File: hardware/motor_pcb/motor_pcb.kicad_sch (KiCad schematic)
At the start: 13 parts

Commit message: Updated schematic
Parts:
- removed J?: Conn_01x13, symbol Connector_Generic:Conn_01x13
- added J1: Conn_01x14, Connector_Hirose:Hirose_DF52-14S-0.8H_1x14-1MP_P0.80mm_Horizontal, symbol Connector_Generic:Conn_01x14
- C1: renamed from C?; footprint (none) -> Capacitor_SMD:C_0805_2012Metric
- C2, C3, C4, C5, C6: renamed from C?; footprint (none) -> Capacitor_SMD:C_0603_1608Metric
- J2: renamed from J?; footprint (none) -> Connector_Hirose:Hirose_DF52-3S-0.8H_1x03-1MP_P0.80mm_Horizontal; LCSC (none) -> C500138
- R1: renamed from R?; value R -> 0.15; footprint (none) -> Resistor_SMD:R_1206_3216Metric
- R2, R3: renamed from R?; footprint (none) -> Resistor_SMD:R_0603_1608Metric
- U1: renamed from U?; footprint Modified:QFN-20-1EP_3x3mm_P0.4mm_EP1.65x1.65mm_ThermalVias_LargerViaHoles -> Package_DFN_QFN:QFN-20-1EP_3x3mm_P0.4mm_EP1.65x1.65mm_ThermalVias
- gave numbers to parts that had none: 1
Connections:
- net +3V3: now also J1.1 (Pin_1)
- net +5V: now also J1.2 (Pin_2)
- net CS: now also J1.12 (Pin_12)
- net DIAG: now also J1.9 (Pin_9)
- net GND: now also J1.13 (Pin_13), J1.14 (Pin_14)
- net SCL: now also J1.11 (Pin_11)
- net SDA: now also J1.10 (Pin_10)
- net UH: now also J1.3 (Pin_3)
- net UL: now also J1.4 (Pin_4)
- net VH: now also J1.5 (Pin_5)
- net VL: now also J1.6 (Pin_6)
- net WH: now also J1.7 (Pin_7)
- net WL: now also J1.8 (Pin_8)
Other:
- note added: "0.15 Ohm -> 1.6A max motor current"

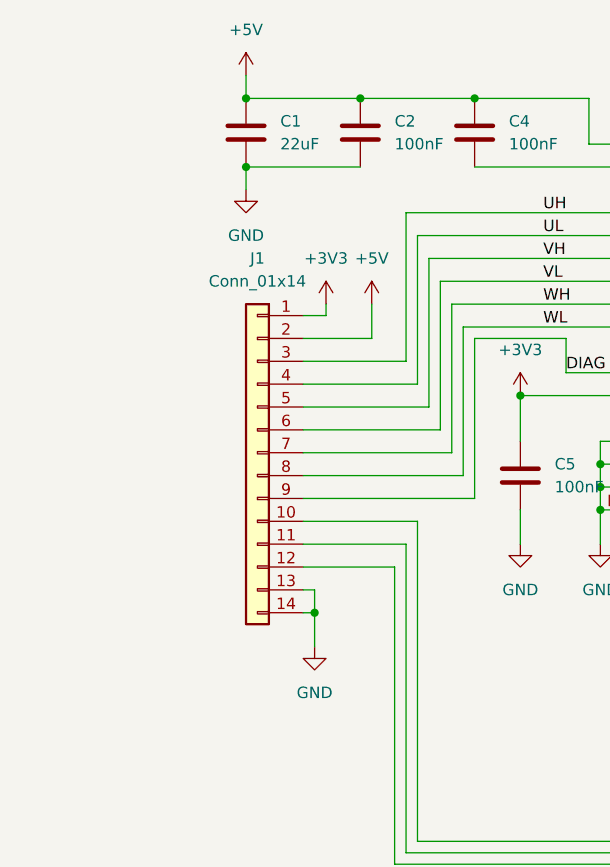
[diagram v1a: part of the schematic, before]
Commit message: Updated power connector
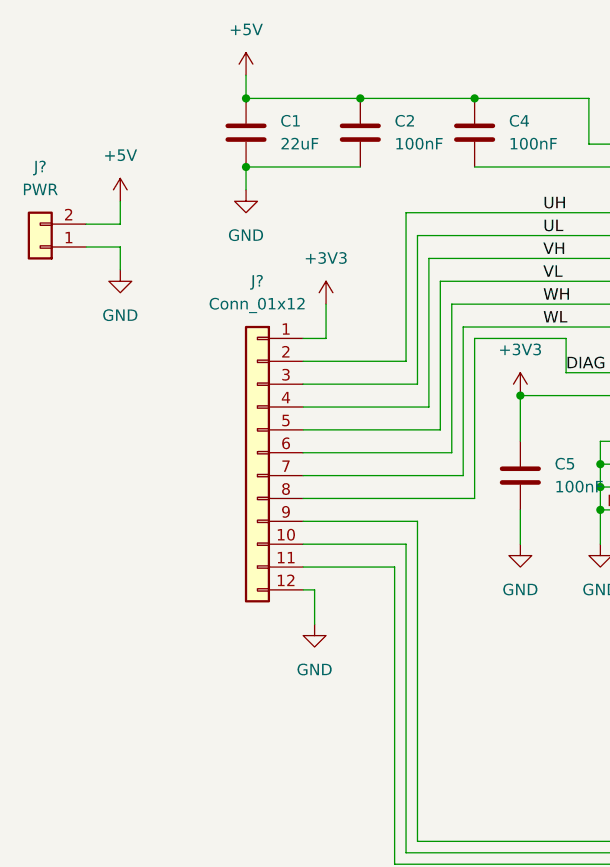
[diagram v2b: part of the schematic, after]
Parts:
- removed J1: Conn_01x14, Connector_Hirose:Hirose_DF52-14S-0.8H_1x14-1MP_P0.80mm_Horizontal, symbol Connector_Generic:Conn_01x14
- added J?: PWR, Connector_PinHeader_2.54mm:PinHeader_1x02_P2.54mm_Vertical, symbol Connector_Generic:Conn_01x02
- added J?: Conn_01x12, Connector_Hirose:Hirose_DF52-12S-0.8H_1x12-1MP_P0.80mm_Horizontal, symbol Connector_Generic:Conn_01x12
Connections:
- net +3V3: now also J?.1 (Pin_1)
- net +5V: now also J?.2 (Pin_2)
- net CS: now also J?.11 (Pin_11)
- net DIAG: now also J?.8 (Pin_8)
- net GND: now also J?.1 (Pin_1), J?.12 (Pin_12)
- net SCL: now also J?.10 (Pin_10)
- net SDA: now also J?.9 (Pin_9)
- net UH: now also J?.2 (Pin_2)
- net UL: now also J?.3 (Pin_3)
- net VH: now also J?.4 (Pin_4)
- net VL: now also J?.5 (Pin_5)
- net WH: now also J?.6 (Pin_6)
- net WL: now also J?.7 (Pin_7)

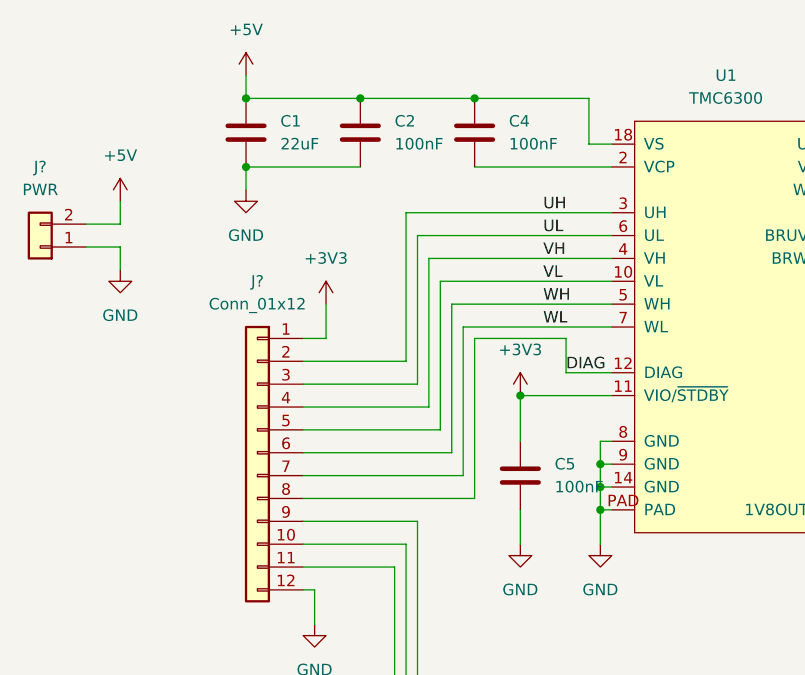
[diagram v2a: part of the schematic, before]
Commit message: Changed to fpc connector
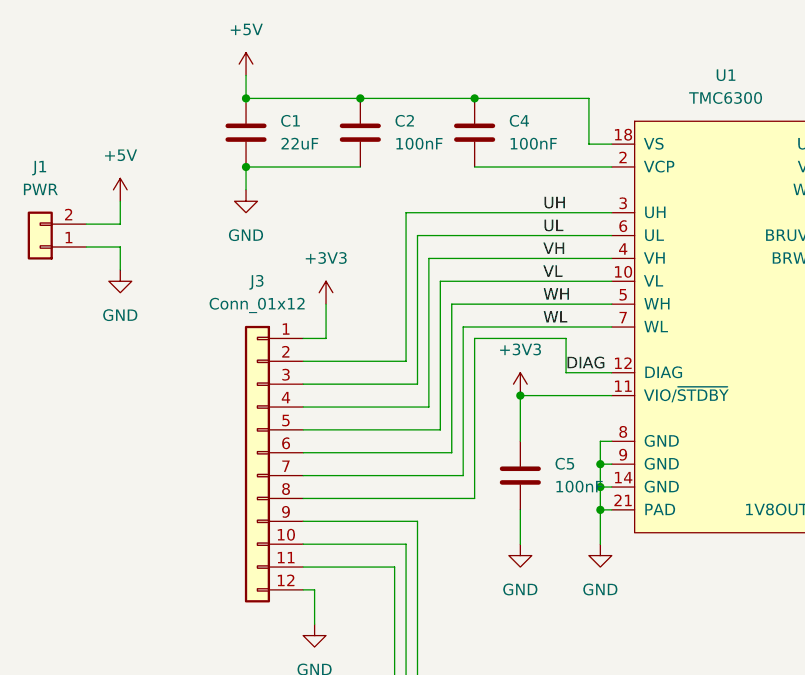
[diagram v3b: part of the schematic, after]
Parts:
- J3: renamed from J?; footprint Connector_Hirose:Hirose_DF52-12S-0.8H_1x12-1MP_P0.80mm_Horizontal -> Jushuo:FPC_12
- gave numbers to parts that had none: 1
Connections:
- net GND: now also U1.21 (PAD); no longer U1.PAD
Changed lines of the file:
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@@
   (symbol (lib_id "Connector_Generic:Conn_01x02") (at 88.9 45.72 180) (unit 1)
     (in_bom yes) (on_board yes) (fields_autoplaced)
-    (property "Reference" "J?" (id 0) (at 88.9 36.83 0))
+    (property "Reference" "J1" (id 0) (at 88.9 36.83 0))
     (property "Value" "PWR" (id 1) (at 88.9 39.37 0))
     (property "Footprint" "Connector_PinHeader_2.54mm:PinHeader_1x02_P2.54mm_Vertical" (id 2) (at 88.9 45.72 0)
@@
   (symbol (lib_id "power:GND") (at 97.79 48.26 0) (unit 1)
     (in_bom yes) (on_board yes) (fields_autoplaced)
-    (property "Reference" "#PWR?" (id 0) (at 97.79 54.61 0)
+    (property "Reference" "#PWR0101" (id 0) (at 97.79 54.61 0)
       (effects (font (size 1.27 1.27)) hide)
     )
@@
   (symbol (lib_id "Connector_Generic:Conn_01x12") (at 113.03 68.58 0) (mirror y) (unit 1)
     (in_bom yes) (on_board yes) (fields_autoplaced)
-    (property "Reference" "J?" (id 0) (at 113.03 49.53 0))
+    (property "Reference" "J3" (id 0) (at 113.03 49.53 0))
     (property "Value" "Conn_01x12" (id 1) (at 113.03 52.07 0))
-    (property "Footprint" "Connector_Hirose:Hirose_DF52-12S-0.8H_1x12-1MP_P0.80mm_Horizontal" (id 2) (at 113.03 68.58 0)
+    (property "Footprint" "Jushuo:FPC_12" (id 2) (at 113.03 68.58 0)
       (effects (font (size 1.27 1.27)) hide)
     )
@@
     (pin "8")
     (pin "9")
-    (pin "PAD")
+    (pin "21")
   )
   (symbol (lib_id "power:GND") (at 143.51 134.62 0) (unit 1)
@@
     )
     (path "/24612733-1d50-42bd-841c-be1f707d056b"
-      (reference "#PWR?") (unit 1) (value "GND") (footprint "")
+      (reference "#PWR0101") (unit 1) (value "GND") (footprint "")
     )
     (path "/8c77fd94-8e4c-4959-8bd9-3052e0edb37f"
@@
       (reference "C6") (unit 1) (value "100nF") (footprint "Capacitor_SMD:C_0603_1608Metric")
     )
+    (path "/03910351-5c5a-4e87-ae00-e0f31c977d99"
+      (reference "J1") (unit 1) (value "PWR") (footprint "Connector_PinHeader_2.54mm:PinHeader_1x02_P2.54mm_Vertical")
+    )
     (path "/a2c13c1a-ecf0-4489-bc67-4ea2d4323322"
       (reference "J2") (unit 1) (value "Conn_01x03") (footprint "Connector_Hirose:Hirose_DF52-3S-0.8H_1x03-1MP_P0.80mm_Horizontal")
     )
-    (path "/03910351-5c5a-4e87-ae00-e0f31c977d99"
-      (reference "J?") (unit 1) (value "PWR") (footprint "Connector_PinHeader_2.54mm:PinHeader_1x02_P2.54mm_Vertical")
-    )
     (path "/beeb3293-b654-424e-b1ea-63ed0fc7ea2d"
-      (reference "J?") (unit 1) (value "Conn_01x12") (footprint "Connector_Hirose:Hirose_DF52-12S-0.8H_1x12-1MP_P0.80mm_Horizontal")
+      (reference "J3") (unit 1) (value "Conn_01x12") (footprint "Jushuo:FPC_12")
     )
     (path "/ef183a37-aa63-490e-aeb2-ec1d529f6328"

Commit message: Updated lcsc number
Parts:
- J3: LCSC C3012324 -> C11051
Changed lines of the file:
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@@
       (effects (font (size 1.27 1.27)) hide)
     )
-    (property "LCSC" "C3012324" (id 4) (at 113.03 68.58 0)
+    (property "LCSC" "C11051" (id 4) (at 113.03 68.58 0)
       (effects (font (size 1.27 1.27)) hide)
     )
@@
     (pin "2")
     (pin "20")
+    (pin "21")
     (pin "3")
     (pin "4")
@@
     (pin "8")
     (pin "9")
-    (pin "21")
   )
   (symbol (lib_id "power:GND") (at 143.51 134.62 0) (unit 1)

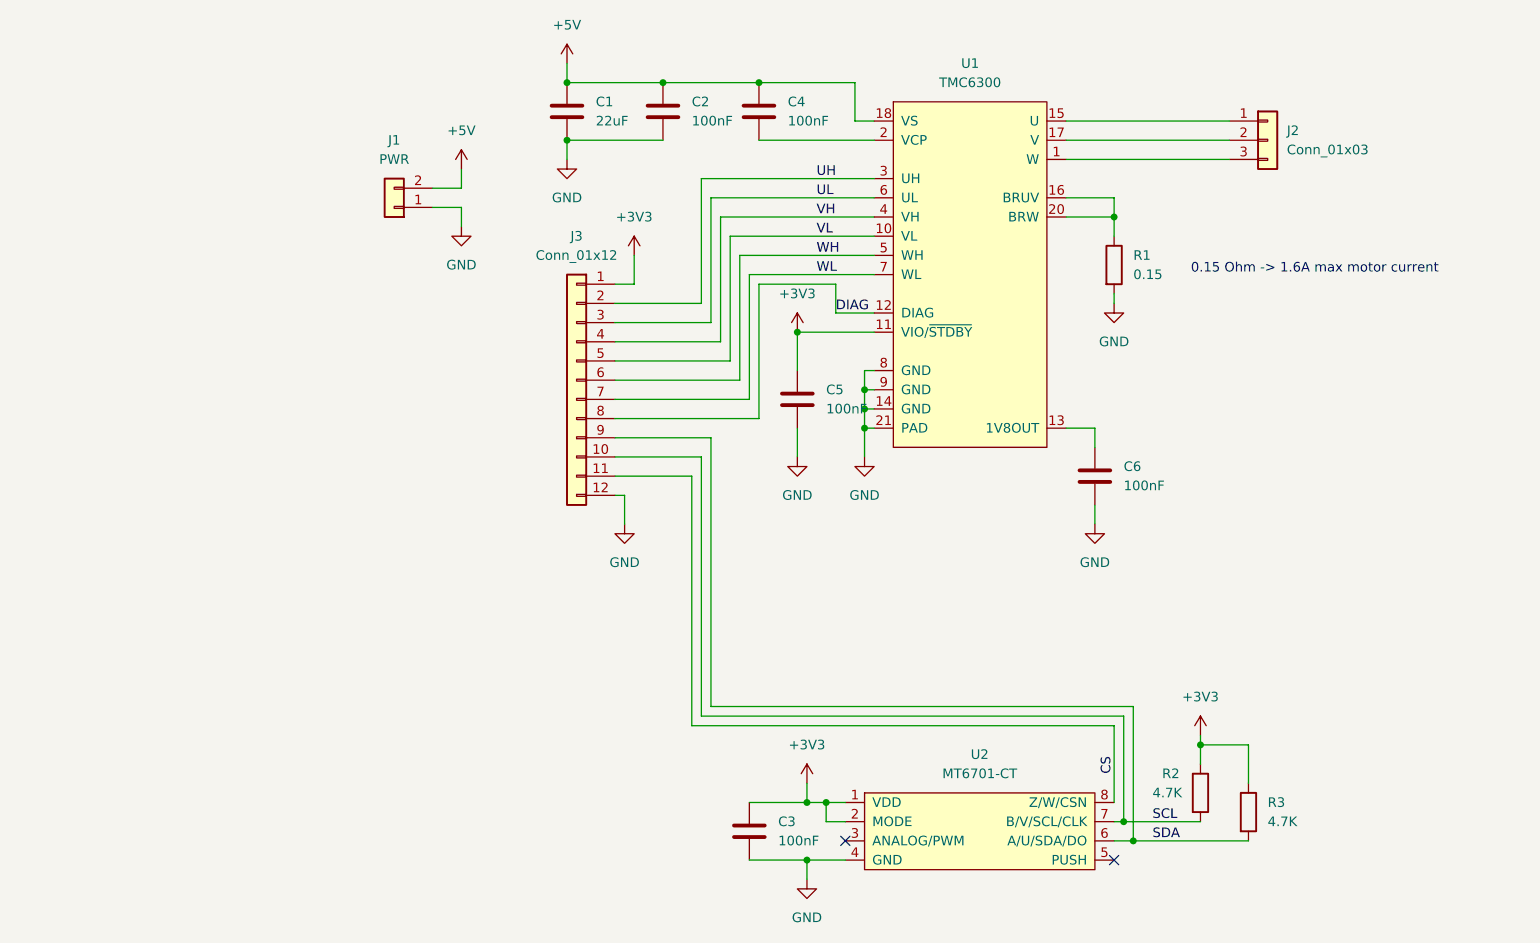
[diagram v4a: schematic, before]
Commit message: Updated design with new wiring structure
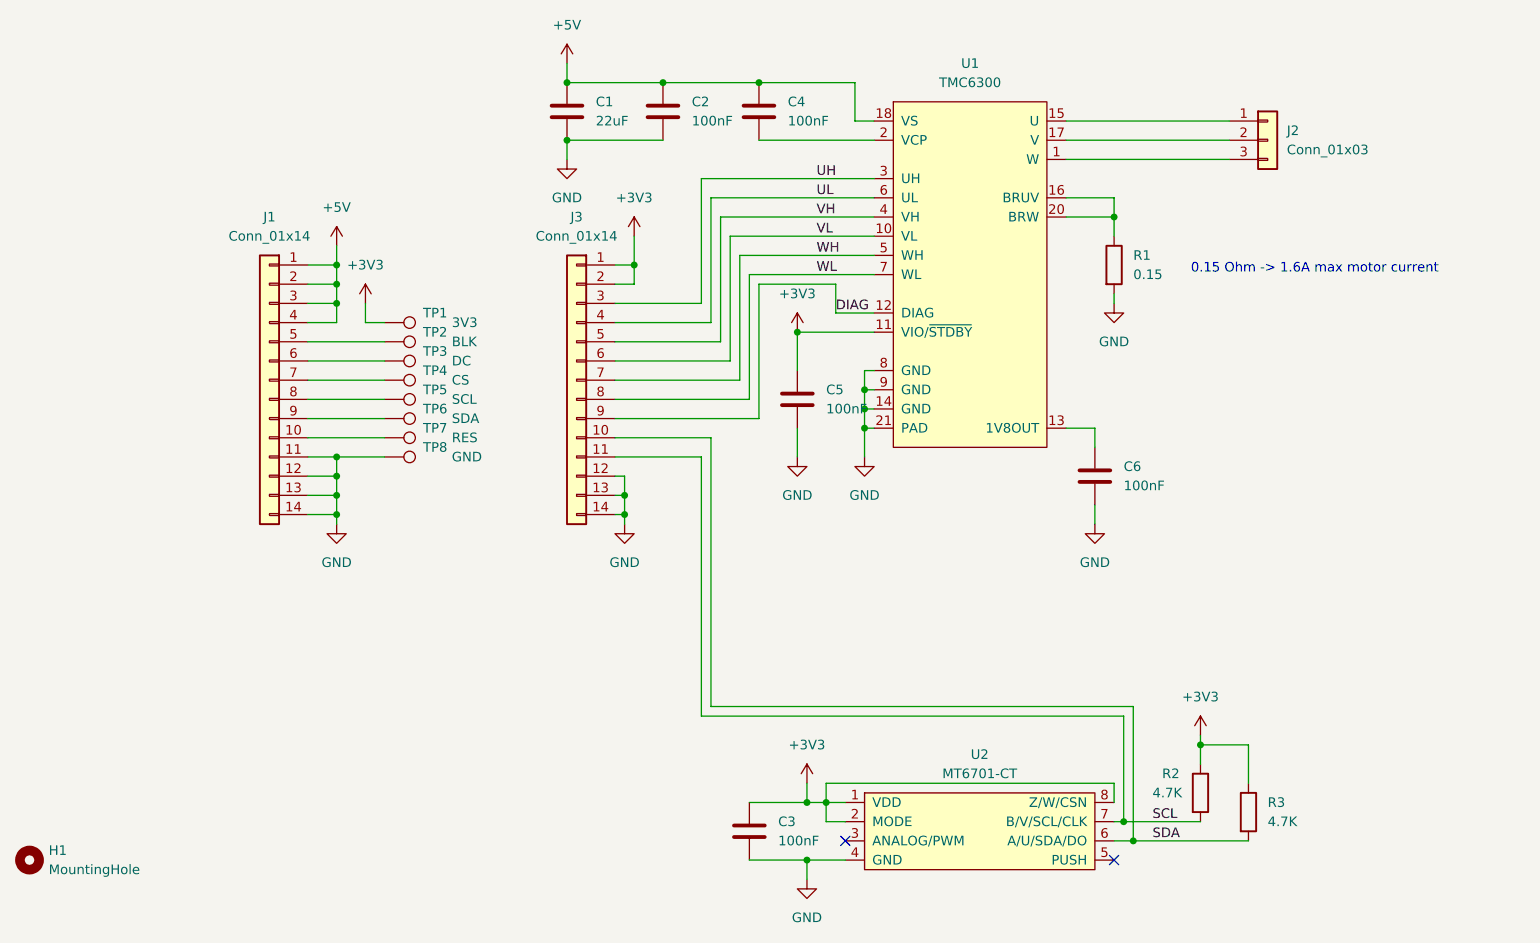
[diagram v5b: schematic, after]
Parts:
- removed J1: PWR, Connector_PinHeader_2.54mm:PinHeader_1x02_P2.54mm_Vertical, symbol Connector_Generic:Conn_01x02
- removed J3: Conn_01x12, Jushuo:FPC_12, symbol Connector_Generic:Conn_01x12
- added H1: MountingHole, Holes:Holes, symbol Mechanical:MountingHole
- added J1, J3: Conn_01x14, Connector_Hirose:Hirose_DF52-14S-0.8H_1x14-1MP_P0.80mm_Horizontal, symbol Connector_Generic:Conn_01x14
- added TP1: 3V3, TestPoint:TestPoint_Pad_2.0x2.0mm, symbol Connector:TestPoint
- added TP2: BLK, TestPoint:TestPoint_Pad_2.0x2.0mm, symbol Connector:TestPoint
- added TP3: DC, TestPoint:TestPoint_Pad_2.0x2.0mm, symbol Connector:TestPoint
- added TP4: CS, TestPoint:TestPoint_Pad_2.0x2.0mm, symbol Connector:TestPoint
- added TP5: SCL, TestPoint:TestPoint_Pad_2.0x2.0mm, symbol Connector:TestPoint
- added TP6: SDA, TestPoint:TestPoint_Pad_2.0x2.0mm, symbol Connector:TestPoint
- added TP7: RES, TestPoint:TestPoint_Pad_2.0x2.0mm, symbol Connector:TestPoint
- added TP8: GND, TestPoint:TestPoint_Pad_2.0x2.0mm, symbol Connector:TestPoint
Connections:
- net CS is gone; now on net +3V3: U2.8 (Z/W/CSN)
- net +3V3: now also J3.1 (Pin_1), J3.2 (Pin_2), TP1.1
- net +5V: now also J1.1 (Pin_1), J1.2 (Pin_2), J1.3 (Pin_3), J1.4 (Pin_4)
- net DIAG: now also J3.9 (Pin_9)
- net GND: now also J1.11 (Pin_11), J1.12 (Pin_12), J1.13 (Pin_13), J1.14 (Pin_14), J3.12 (Pin_12), J3.13 (Pin_13), J3.14 (Pin_14), TP8.1
- net SCL: now also J3.11 (Pin_11)
- net SDA: now also J3.10 (Pin_10)
- net UH: now also J3.3 (Pin_3)
- net UL: now also J3.4 (Pin_4)
- net VH: now also J3.5 (Pin_5)
- net VL: now also J3.6 (Pin_6)
- net WH: now also J3.7 (Pin_7)
- net WL: now also J3.8 (Pin_8)
- new net: J1.6 (Pin_6), TP3.1
- new net: J1.10 (Pin_10), TP7.1
- new net: J1.5 (Pin_5), TP2.1
- new net: J1.7 (Pin_7), TP4.1
- new net: J1.8 (Pin_8), TP5.1
- new net: J1.9 (Pin_9), TP6.1

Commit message: Updated connectors
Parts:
- J1, J3: footprint Connector_Hirose:Hirose_DF52-14S-0.8H_1x14-1MP_P0.80mm_Horizontal -> Jushuo:FPC_14; LCSC (none) -> C262561
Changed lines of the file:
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@@
     (property "Reference" "J1" (id 0) (at 72.39 46.99 0))
     (property "Value" "Conn_01x14" (id 1) (at 72.39 49.53 0))
-    (property "Footprint" "Connector_Hirose:Hirose_DF52-14S-0.8H_1x14-1MP_P0.80mm_Horizontal" (id 2) (at 72.39 68.58 0)
+    (property "Footprint" "Jushuo:FPC_14" (id 2) (at 72.39 68.58 0)
       (effects (font (size 1.27 1.27)) hide)
     )
     (property "Datasheet" "~" (id 3) (at 72.39 68.58 0)
+      (effects (font (size 1.27 1.27)) hide)
+    )
+    (property "LCSC" "C262561" (id 4) (at 72.39 68.58 0)
       (effects (font (size 1.27 1.27)) hide)
     )
@@
     (property "Reference" "J3" (id 0) (at 113.03 46.99 0))
     (property "Value" "Conn_01x14" (id 1) (at 113.03 49.53 0))
-    (property "Footprint" "Connector_Hirose:Hirose_DF52-14S-0.8H_1x14-1MP_P0.80mm_Horizontal" (id 2) (at 113.03 68.58 0)
+    (property "Footprint" "Jushuo:FPC_14" (id 2) (at 113.03 68.58 0)
       (effects (font (size 1.27 1.27)) hide)
     )
     (property "Datasheet" "~" (id 3) (at 113.03 68.58 0)
+      (effects (font (size 1.27 1.27)) hide)
+    )
+    (property "LCSC" "C262561" (id 4) (at 113.03 68.58 0)
       (effects (font (size 1.27 1.27)) hide)
     )
@@
     )
     (path "/6a143197-35f1-45ab-830a-141703a65122"
-      (reference "J1") (unit 1) (value "Conn_01x14") (footprint "Connector_Hirose:Hirose_DF52-14S-0.8H_1x14-1MP_P0.80mm_Horizontal")
+      (reference "J1") (unit 1) (value "Conn_01x14") (footprint "Jushuo:FPC_14")
     )
     (path "/a2c13c1a-ecf0-4489-bc67-4ea2d4323322"
@@
     )
     (path "/b35cb3e6-6a87-48f6-ac20-a263fc6cc2f3"
-      (reference "J3") (unit 1) (value "Conn_01x14") (footprint "Connector_Hirose:Hirose_DF52-14S-0.8H_1x14-1MP_P0.80mm_Horizontal")
+      (reference "J3") (unit 1) (value "Conn_01x14") (footprint "Jushuo:FPC_14")
     )
     (path "/ef183a37-aa63-490e-aeb2-ec1d529f6328"
